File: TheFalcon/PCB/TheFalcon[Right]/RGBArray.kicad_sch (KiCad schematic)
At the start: 57 parts, among them IC1 IS31FL3729-QFLS4-TR

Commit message: Save
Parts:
- added J8: Conn_01x01, Connector_Wire:SolderWirePad_1x01_SMD_1x2mm, symbol Connector_Generic:Conn_01x01
- added R23: 0, Resistor_SMD:R_0603_1608Metric_Pad0.98x0.95mm_HandSolder, symbol Device:R
- renumbered C14 to C15, C12 to C16, C13 to C17, R9 to R1, R11 to R10, R14 to R11, R17 to R14, R20 to R17, R6 to R2, R23 to R20, R5 to R8, R10 to R9, RGB37 to RGB36
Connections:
- net +5V: now also J8.1 (Pin_1); no longer IC1.28 (AD)
- net CS1: now also R20.2; no longer R1.2
- net CS2: now also R21.2; no longer R9.2
- net CS3: now also R22.2; no longer R10.2
- net CS7: now also R1.2; no longer R20.2
- net CS8: now also R9.2; no longer R21.2
- net CS9: now also R10.2; no longer R22.2
- net GND: now also R23.1
- new net AD: IC1.28 (AD), R23.2
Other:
- note added: "5V to change AD address if needed"

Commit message: Right Side Done
Need to check but right side looks good
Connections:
- net SW1: now also RGB11.2 (COM_A), RGB18.2 (COM_A), RGB25.2 (COM_A), RGB32.2 (COM_A), RGB4.2 (COM_A); no longer RGB36.2 (COM_A)
- net SW2: now also RGB12.2 (COM_A), RGB19.2 (COM_A), RGB26.2 (COM_A), RGB33.2 (COM_A), RGB5.2 (COM_A); no longer RGB14.2 (COM_A), RGB21.2 (COM_A), RGB28.2 (COM_A), RGB35.2 (COM_A), RGB7.2 (COM_A)
- net SW4: now also RGB14.2 (COM_A), RGB21.2 (COM_A), RGB28.2 (COM_A), RGB35.2 (COM_A), RGB7.2 (COM_A); no longer RGB12.2 (COM_A), RGB19.2 (COM_A), RGB26.2 (COM_A), RGB33.2 (COM_A), RGB5.2 (COM_A)
- net SW5: now also RGB36.2 (COM_A); no longer RGB11.2 (COM_A), RGB18.2 (COM_A), RGB25.2 (COM_A), RGB32.2 (COM_A), RGB4.2 (COM_A)
- net SW6: now also RGB1.2 (COM_A), RGB15.2 (COM_A), RGB22.2 (COM_A), RGB29.2 (COM_A), RGB8.2 (COM_A); no longer RGB10.2 (COM_A), RGB17.2 (COM_A), RGB24.2 (COM_A), RGB3.2 (COM_A), RGB31.2 (COM_A)
- net SW8: now also RGB10.2 (COM_A), RGB17.2 (COM_A), RGB24.2 (COM_A), RGB3.2 (COM_A), RGB31.2 (COM_A); no longer RGB1.2 (COM_A), RGB15.2 (COM_A), RGB22.2 (COM_A), RGB29.2 (COM_A), RGB8.2 (COM_A)
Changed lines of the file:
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@@
+		)
+	)
+	(label "SW4"
+		(at 76.2 25.4 0)
+		(effects
+			(font
+				(size 1.27 1.27)
+			)
+			(justify left bottom)
 		)
 	)
@@
 		)
 	)
+	(label "SW5"
+		(at 86.36 25.4 0)
+		(effects
+			(font
+				(size 1.27 1.27)
+			)
+			(justify left bottom)
+		)
+	)
 	(label "SW7"
 		(at 25.4 25.4 0)
@@
 		)
 	)
-	(label "SW5"
-		(at 45.72 25.4 0)
-		(effects
-			(font
-				(size 1.27 1.27)
-			)
-			(justify left bottom)
-		)
-	)
 	(label "CS6"
 		(at 106.68 91.44 0)
@@
 		)
 	)
-	(label "SW4"
-		(at 55.88 25.4 0)
-		(effects
-			(font
-				(size 1.27 1.27)
-			)
-			(justify left bottom)
-		)
-	)
 	(label "CS7"
 		(at 102.87 31.75 0)
@@
 		)
 	)
+	(label "SW2"
+		(at 55.88 25.4 0)
+		(effects
+			(font
+				(size 1.27 1.27)
+			)
+			(justify left bottom)
+		)
+	)
 	(label "CS12"
 		(at 113.03 158.75 0)
@@
 		)
 	)
-	(label "SW2"
-		(at 76.2 25.4 0)
-		(effects
-			(font
-				(size 1.27 1.27)
-			)
-			(justify left bottom)
-		)
-	)
 	(label "CS5"
 		(at 171.45 58.42 180)
@@
 		)
 	)
-	(label "SW1"
-		(at 86.36 25.4 0)
-		(effects
-			(font
-				(size 1.27 1.27)
-			)
-			(justify left bottom)
-		)
-	)
 	(label "CS11"
 		(at 171.45 73.66 180)
@@
 		)
 	)
+	(label "SW1"
+		(at 45.72 25.4 0)
+		(effects
+			(font
+				(size 1.27 1.27)
+			)
+			(justify left bottom)
+		)
+	)
 	(label "AD"
 		(at 227.33 48.26 0)
@@
 		)
 	)
+	(label "SW8"
+		(at 35.56 25.4 0)
+		(effects
+			(font
+				(size 1.27 1.27)
+			)
+			(justify left bottom)
+		)
+	)
 	(label "G_RGB_ROW_1"
 		(at 93.98 88.9 180)
@@
 	)
 	(label "SW6"
-		(at 35.56 25.4 0)
+		(at 15.24 25.4 0)
 		(effects
 			(font
@@
 		)
 	)
-	(label "SW8"
-		(at 15.24 25.4 0)
-		(effects
-			(font
-				(size 1.27 1.27)
-			)
-			(justify left bottom)
-		)
-	)

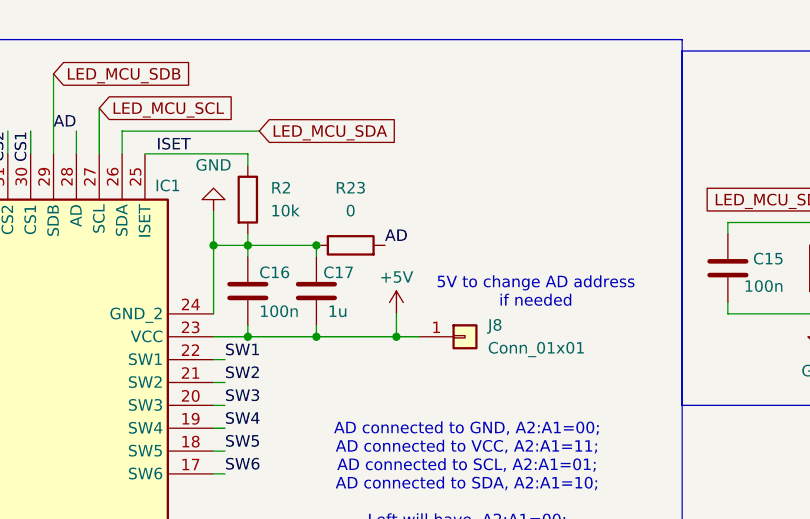
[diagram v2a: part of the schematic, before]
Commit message: Files ready for production
Going to panelise seperate files to reduce PCBA cost
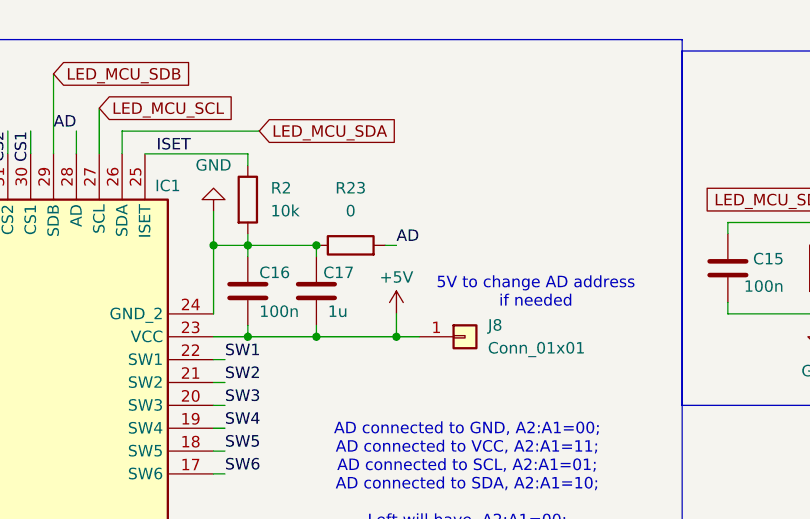
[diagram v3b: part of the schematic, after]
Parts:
- C15, C16: LCSC Part Number (none) -> C1525
- C17: LCSC Part Number (none) -> C1592
- IC1: Arrow Part Number IS31FL3729-QFLS4-TR -> (none); Arrow Price/Stock https://www.arrow.com/en/products/is31fl3729-qfls4-tr/integ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 -> (none); Height 0.8 -> (none); LCSC Part Number (none) -> C2940549; Manufacturer_Name Lumissil Microsystems -> (none); Manufacturer_Part_Number IS31FL3729-QFLS4-TR -> (none); Mouser Part Number 870-IS31FL3729QFLS4T -> (none); Mouser Price/Stock https://www.mouser.com/Search/Refine.aspx?Keyword=870-IS31F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 -> (none)
- R1, R11, R12, R14, R15, R17, R18, R20, R21, R9: LCSC Part Number (none) -> C22950
- R10, R13, R16, R19, R22: LCSC Part Number (none) -> C17738
- R2: LCSC Part Number (none) -> C15401
- R23: LCSC Part Number (none) -> C17477
- R8: LCSC Part Number (none) -> C14675
- RGB1, RGB10, RGB11, RGB12, RGB13, RGB14, RGB15, RGB16, RGB17, RGB18, RGB19, RGB2, RGB20, RGB21, RGB22, RGB23, RGB24, RGB25, RGB26, RGB27, RGB28, RGB29, RGB3, RGB30, RGB31, RGB32, RGB33, RGB34, RGB35, RGB36, RGB4, RGB5, RGB6, RGB7, RGB8, RGB9: Height 1.95 -> (none); Link https://www.digikey.co.za/en/products/detail/harvatek-corpo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 -> (none); Manufacturer_Name Harvatek -> (none); Manufacturer_Part_Number T36K3BGR-05D000121U1930 -> (none)
